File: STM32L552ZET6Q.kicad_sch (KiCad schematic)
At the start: 26 parts, among them SW501 MCU_RST, U501 STM32L552ZET6Q, Y501 32.768kHz, 1.2pF, Y502 16MHz, 7pF

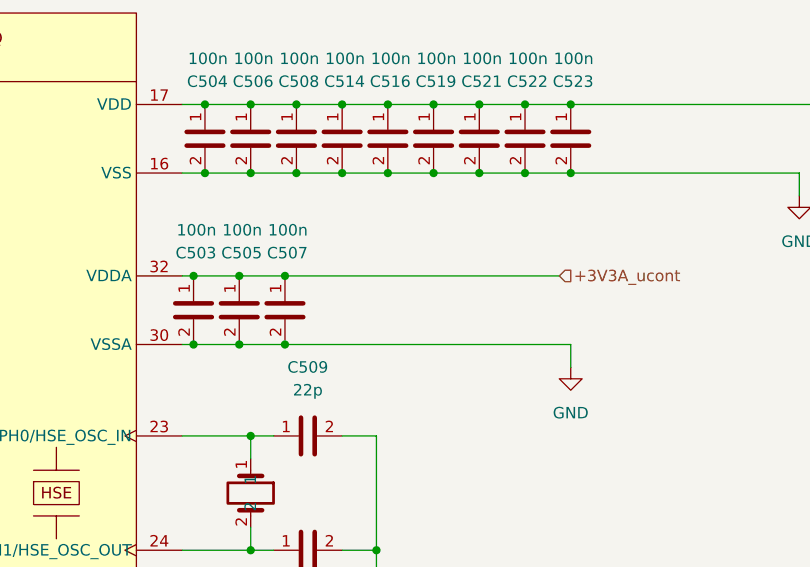
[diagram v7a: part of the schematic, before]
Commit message: slimed out gpio conns, changed to 6layer
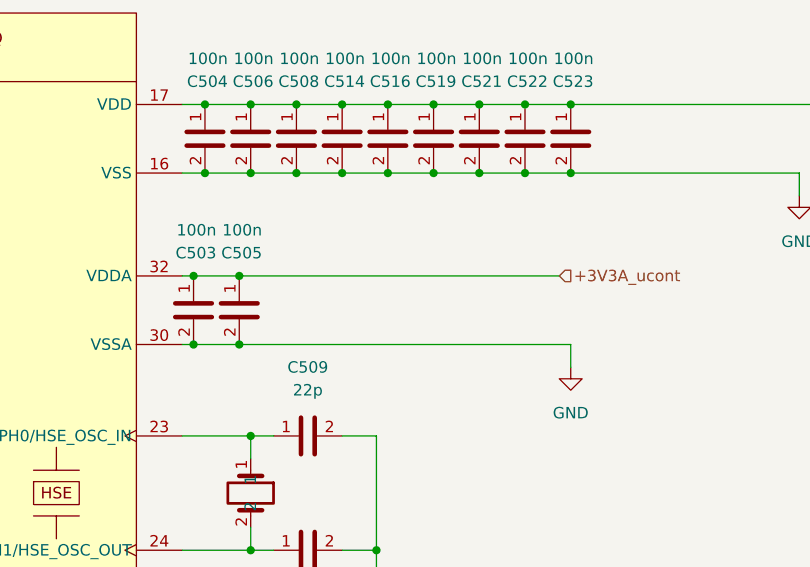
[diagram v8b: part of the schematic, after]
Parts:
- removed C507: 100n, Capacitor_SMD:C_0402_1005Metric_Pad0.74x0.62mm_HandSolder, symbol bfr_capacitors:CL05B104KB54PNC
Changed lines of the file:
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@@
-	)
-	(junction
-		(at 132.08 58.42)
-		(diameter 0)
-		(color 0 0 0 0)
-	)
-	(junction
-		(at 132.08 50.8)
-		(diameter 0)
-		(color 0 0 0 0)
 	)
 	(junction
@@
 	(wire
 		(pts
-			(xy 127 58.42) (xy 132.08 58.42)
-		)
-		(stroke
-			(width 0)
-			(type default)
-		)
-	)
-	(wire
-		(pts
 			(xy 41.91 81.28) (xy 41.91 85.09)
 		)
@@
 	(wire
 		(pts
-			(xy 132.08 50.8) (xy 162.56 50.8)
-		)
-		(stroke
-			(width 0)
-			(type default)
-		)
-	)
-	(wire
-		(pts
 			(xy 242.57 111.76) (xy 232.41 111.76)
 		)
@@
 	(wire
 		(pts
-			(xy 127 50.8) (xy 132.08 50.8)
+			(xy 127 50.8) (xy 162.56 50.8)
 		)
 		(stroke
@@
 	(wire
 		(pts
-			(xy 132.08 58.42) (xy 163.83 58.42)
+			(xy 127 58.42) (xy 163.83 58.42)
 		)
 		(stroke
@@
 					(unit 1)
 				)
-			)
-		)
-	)
-	(symbol
-		(lib_id "bfr_capacitors:CL05B104KB54PNC")
-		(at 132.08 54.61 0)
-		(unit 1)
-		(exclude_from_sim no)
-		(in_bom yes)
-		(on_board yes)
-		(dnp no)
-		(property "Reference" "C507"
-			(at 134.62 48.26 0)
-			(effects
-				(font
-					(size 1.27 1.27)
-				)
-				(justify right)
-			)
-		)
-		(property "Value" "100n"
-			(at 134.62 45.72 0)
-			(effects
-				(font
-					(size 1.27 1.27)
-				)
-				(justify right)
-			)
-		)
-		(property "Footprint" "Capacitor_SMD:C_0402_1005Metric_Pad0.74x0.62mm_HandSolder"
-			(at 132.08 57.15 0)
-			(effects
-				(font
-					(size 1.27 1.27)
-				)
-				(hide yes)
-			)
-		)
-		(property "Datasheet" ""
-			(at 132.08 58.42 0)
-			(effects
-				(font
-					(size 1.27 1.27)
-				)
-				(hide yes)
-			)
-		)
-		(property "Description" "100nF±10% X7R 50V JLCPCB Basic 0402 Capacitor"
-			(at 132.08 54.61 0)
-			(effects
-				(font
-					(size 1.27 1.27)
-				)
-				(hide yes)
-			)
-		)
-		(property "Sim.Device" "SUBCKT"
-			(at 132.08 59.69 0)
-			(effects
-				(font
-					(size 1.27 1.27)
-				)
-				(hide yes)
-			)
-		)
-		(property "Sim.Pins" "1=P1 2=P2"
-			(at 132.08 60.96 0)
-			(effects
-				(font
-					(size 1.27 1.27)
-				)
-				(hide yes)
-			)
-		)
-		(property "Sim.Library" "${BFRUH_DIR}/Electronics/spice_models/bfr_capacitors/CL05B104KB54PNC.lib"
-			(at 132.08 62.23 0)
-			(effects
-				(font
-					(size 1.27 1.27)
-				)
-				(hide yes)
-			)
-		)
-		(property "Sim.Name" "CL05B104KB54PNC"
-			(at 132.08 63.5 0)
-			(effects
-				(font
-					(size 1.27 1.27)
-				)
-				(hide yes)
-			)
-		)
-		(property "Pretty Name" "100nF X7R 50V 0402 Capacitor"
-			(at 132.08 64.77 0)
-			(effects
-				(font
-					(size 1.27 1.27)
-				)
-				(hide yes)
-			)
-		)
-		(property "Qty/Unit" ""
-			(at 132.08 66.04 0)
-			(effects
-				(font
-					(size 1.27 1.27)
-				)
-				(hide yes)
-			)
-		)
-		(property "Cost/Unit" ""
-			(at 132.08 67.31 0)
-			(effects
-				(font
-					(size 1.27 1.27)
-				)
-				(hide yes)
-			)
-		)
-		(property "Order From" "LCSC"
-			(at 132.08 68.58 0)
-			(effects
-				(font
-					(size 1.27 1.27)
-				)
-				(hide yes)
-			)
-		)
-		(property "Digikey P/N" ""
-			(at 132.08 69.85 0)
-			(effects
-				(font
-					(size 1.27 1.27)
-				)
-				(hide yes)
-			)
-		)
-		(property "Mouser P/N" ""
-			(at 132.08 69.85 0)
-			(effects
-				(font
-					(size 1.27 1.27)
-				)
-				(hide yes)
-			)
-		)
-		(property "LCSC P/N" "C307331"
-			(at 132.08 69.85 0)
-			(effects
-				(font
-					(size 1.27 1.27)
-				)
-				(hide yes)
-			)
-		)
-		(property "JLCPCB Basic Part" "Yes"
-			(at 132.08 69.85 0)
-			(effects
-				(font
-					(size 1.27 1.27)
-				)
-				(hide yes)
-			)
-		)
-		(property "Created by" "capacitor_generator.py script using jlcbasic_additional_capacitor_spec.txt"
-			(at 132.08 69.85 0)
-			(effects
-				(font
-					(size 1.27 1.27)
-				)
-				(hide yes)
-			)
-		)
-		(pin "2"
-		)
-		(pin "1"
-		)
-		(instances
-			(project "DU UC V1 - Minnow"
-				(path "/0aeff2df-21bc-4c76-95d6-83ff8577a8db/479988e2-73e3-4e6d-8b3c-5b8d2874850c"
-					(reference "C507")
-					(unit 1)
-				)
